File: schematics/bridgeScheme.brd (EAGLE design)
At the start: 100 x 80 mm, 22 parts

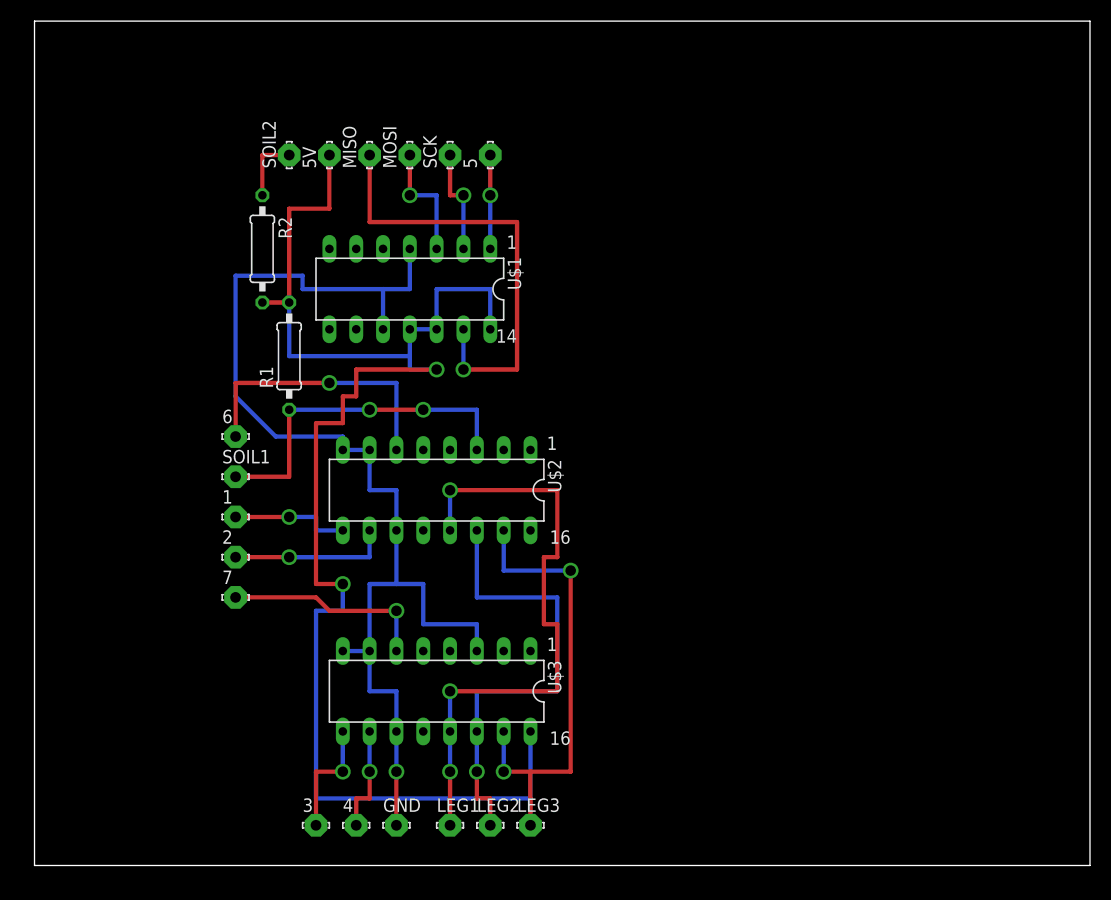
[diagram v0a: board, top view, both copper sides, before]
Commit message: Дал имена всем сигналам, исправил две ошибки на плате, утолщил и переразвел некоторые сигналы без переходных отверстий. (Строго говоря всеравно с ними, но они теперь в ножках микросхем)
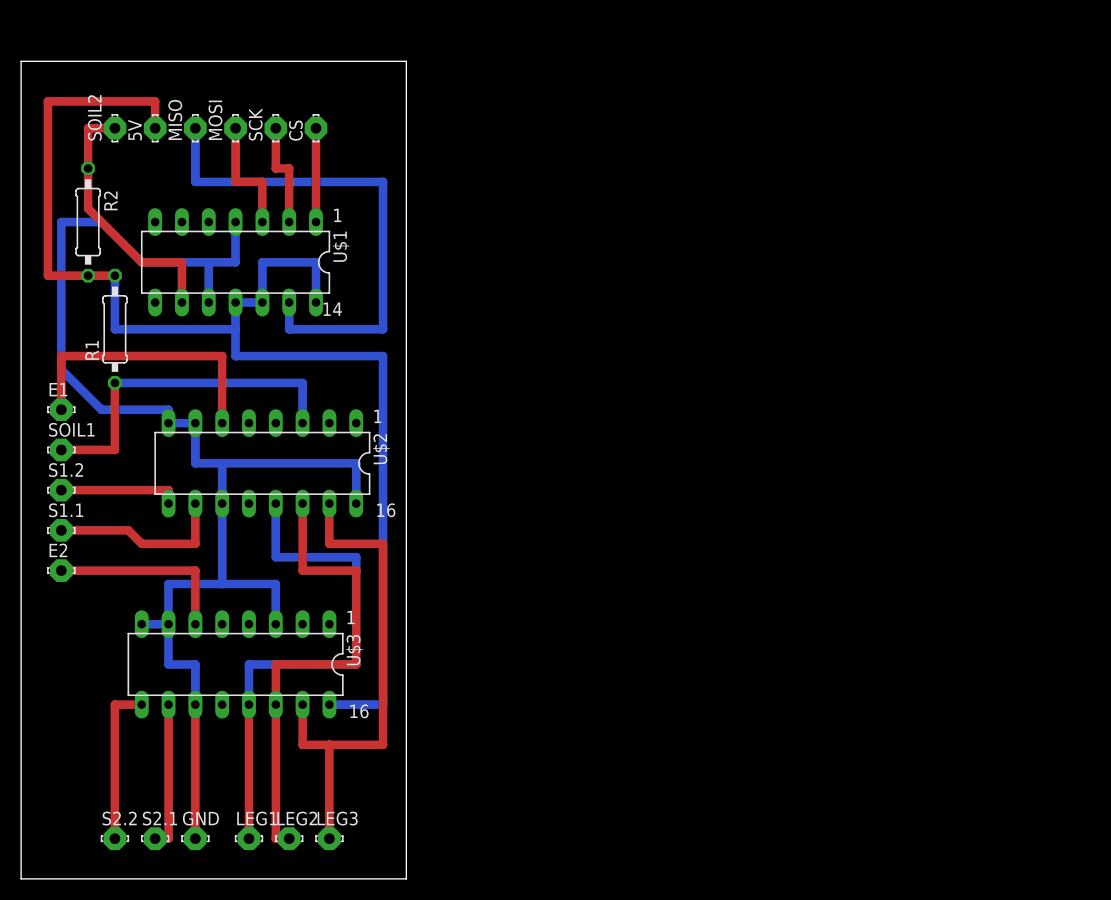
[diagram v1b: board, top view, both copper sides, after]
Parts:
- removed 1, 2, 3, 4, 5, 6, 7: LSP10, solpad:LSP10
- added CS, E1, E2, S1.1, S1.2, S2.1, S2.2: LSP10, solpad:LSP10
- moved U$3 19.2 mm to (19.1, 19.1)
- moved LEG2 19.1 mm to (24.1, 2.54)
- moved LEG3 19.1 mm to (27.9, 2.54)
- moved GND 19.1 mm to (15.2, 2.54)
- moved LEG1 19.1 mm to (20.3, 2.54)
- moved 5V 16.7 mm to (11.4, 69.8)
- moved MOSI 16.7 mm to (19.1, 69.8)
- moved SOIL1 16.7 mm to (2.54, 39.4)
- moved U$1 16.7 mm to (19.1, 57.1)
- moved U$2 16.7 mm to (21.6, 38.1)
- moved MISO 16.7 mm to (15.2, 69.8)
- moved R1 16.7 mm to (7.62, 50.8)
- moved R2 16.7 mm to (5.08, 61.0)
- moved SCK 16.7 mm to (22.9, 69.8)
- moved SOIL2 16.7 mm to (7.62, 69.8)
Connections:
- net N$13 renamed SOIL-1
- net N$15 renamed MISO
- net N$19 renamed SCK
- net N$20 renamed MOSI
- removed net N$18: 5.MP, U$1.1
- removed net N$2: 3.MP, U$3.9
- removed net N$3: 4.MP, U$3.10
- removed net N$4: 2.MP, U$2.10
- removed net N$5: 1.MP, U$2.9
- removed net N$6: 6.MP, U$2.6
- removed net N$7: 7.MP, U$3.6
- removed net N$9: R2.1, SOIL2.MP
- new net CS: CS.MP, U$1.1
- new net E1: E1.MP, U$2.6
- new net E2: E2.MP, U$3.6
- new net S1.1: S1.1.MP, U$2.10
- new net S1.2: S1.2.MP, U$2.9
- new net S2.1: S2.1.MP, U$3.10
- new net S2.2: S2.2.MP, U$3.9
- new net SOIL-2: R2.1, SOIL2.MP, U$1.9
- net GND: now also U$2.16
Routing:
- net E1: track 0.00 -> 26.7 mm
- net N$6: track 26.7 -> 0.00 mm, vias 1 -> 0
- net SOIL-2: track 0.00 -> 25.0 mm
- net GND: track 112.1 -> 132.7 mm, vias 1 -> 0
- net N$7: track 19.6 -> 0.00 mm, vias 1 -> 0
- net 5V: track 142.2 -> 124.5 mm, vias 2 -> 0
- net E2: track 0.00 -> 17.8 mm
- net S1.1: track 0.00 -> 17.0 mm
- net S2.2: track 0.00 -> 15.2 mm
- net N$4: track 15.2 -> 0.00 mm, vias 1 -> 0
- net S2.1: track 0.00 -> 14.0 mm
- net S1.2: track 0.00 -> 11.4 mm
- net N$5: track 11.4 -> 0.00 mm, vias 1 -> 0
- net N$2: track 11.4 -> 0.00 mm, vias 1 -> 0
- net N$3: track 10.2 -> 0.00 mm, vias 1 -> 0
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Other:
- board size 100 x 80 mm -> 36.5 x 77.5 mm
